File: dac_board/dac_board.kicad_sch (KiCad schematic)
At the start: 1 part, among them J1 AudioJack3_Ground

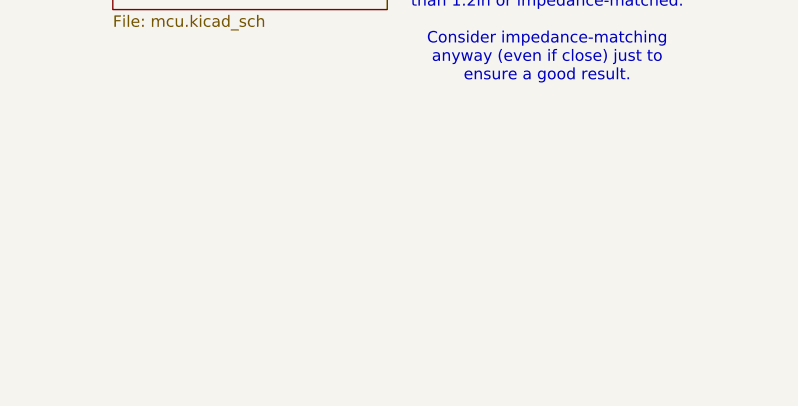
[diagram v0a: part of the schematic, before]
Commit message: Updated USB section to include compliant power management
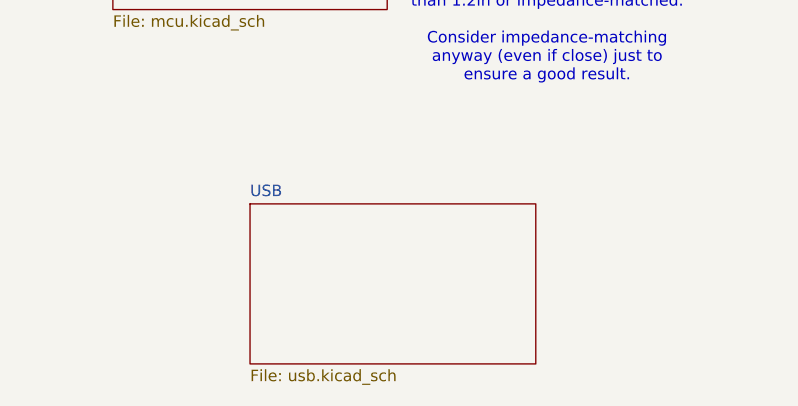
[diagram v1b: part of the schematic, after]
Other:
- added sheet USB (usb.kicad_sch)
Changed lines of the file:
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@@
+		)
+	)
+	(sheet
+		(at 77.47 134.62)
+		(size 31.75 17.78)
+		(exclude_from_sim no)
+		(in_bom yes)
+		(on_board yes)
+		(dnp no)
+		(fields_autoplaced yes)
+		(stroke
+			(width 0.1524)
+			(type solid)
+		)
+		(fill
+			(color 0 0 0 0.0000)
+		)
+		(property "Sheetname" "USB"
+			(at 77.47 133.9084 0)
+			(effects
+				(font
+					(size 1.27 1.27)
+				)
+				(justify left bottom)
+			)
+		)
+		(property "Sheetfile" "usb.kicad_sch"
+			(at 77.47 152.9846 0)
+			(effects
+				(font
+					(size 1.27 1.27)
+				)
+				(justify left top)
+			)
+		)
+		(instances
+			(project "dac_board"
+				(path "/387b6079-e547-4b62-84b5-51a54c04db0a"
+					(page "7")
+				)
+			)
 		)
 	)

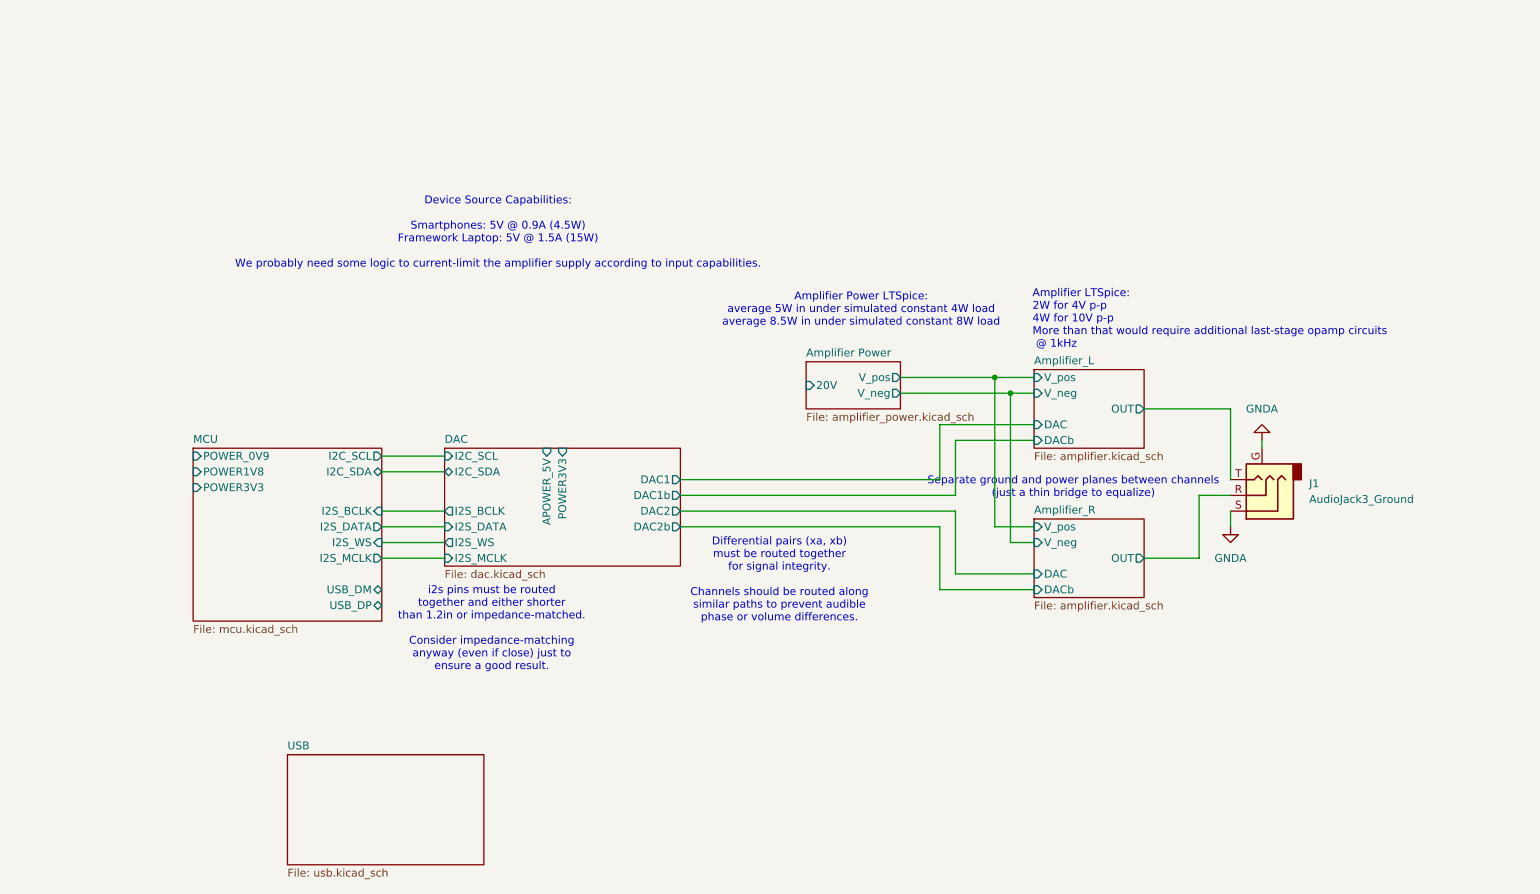
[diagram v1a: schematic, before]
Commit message: Wired up USB and USB-PD to MCU
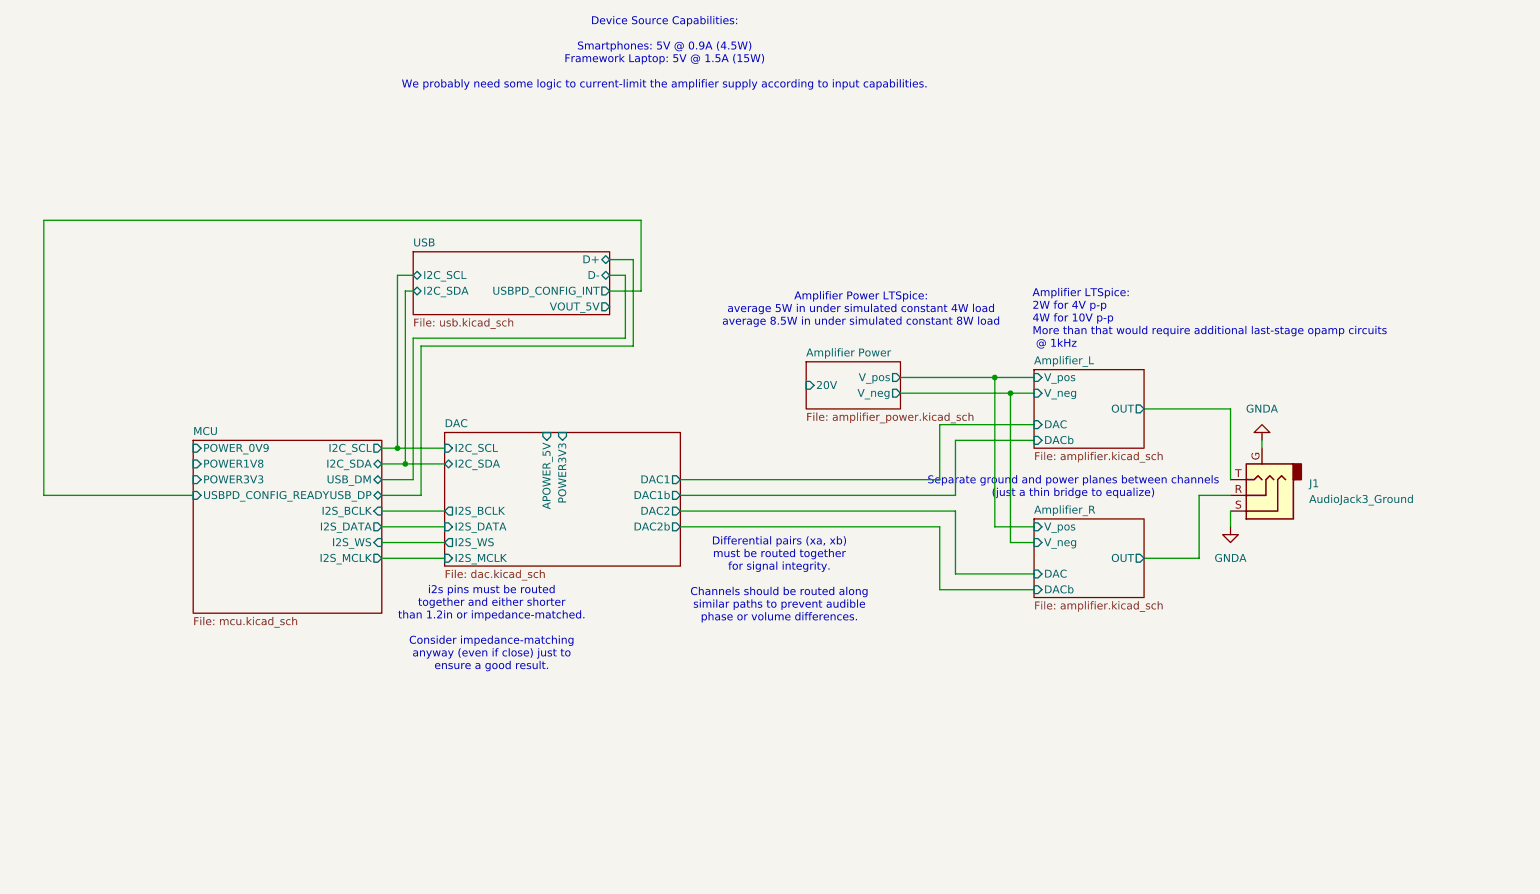
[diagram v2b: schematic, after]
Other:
- sheet MCU ports: added USBPD_CONFIG_READY; removed none
- sheet USB ports: added D+, D-, I2C_SCL, I2C_SDA, USBPD_CONFIG_INT, VOUT_5V; removed none

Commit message: Added power supplies. First complete schematic draft.
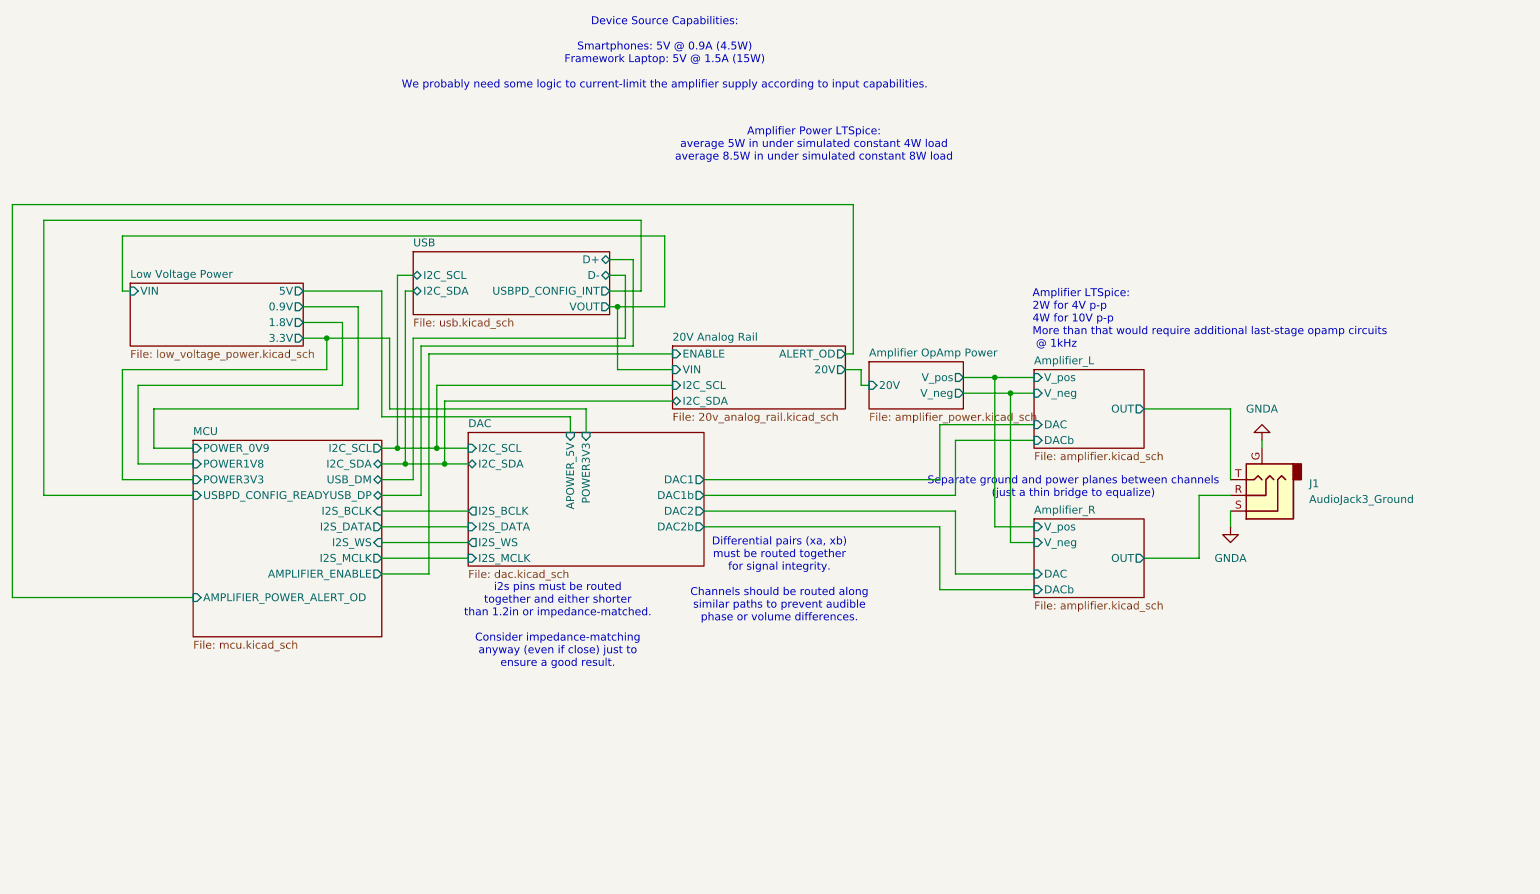
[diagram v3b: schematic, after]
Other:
- sheet Amplifier Power renamed Amplifier OpAmp Power
- added sheet 20V Analog Rail (20v_analog_rail.kicad_sch)
- added sheet Low Voltage Power (low_voltage_power.kicad_sch)
- sheet MCU ports: added AMPLIFIER_ENABLE, AMPLIFIER_POWER_ALERT_OD; removed none
- sheet USB ports: added VOUT; removed VOUT_5V
